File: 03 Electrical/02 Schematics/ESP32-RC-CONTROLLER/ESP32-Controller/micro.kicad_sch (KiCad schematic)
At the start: 3 parts, among them J2 USB_C_Receptacle_USB2.0_14P, U1 ESP32-C3, U3 CH340C

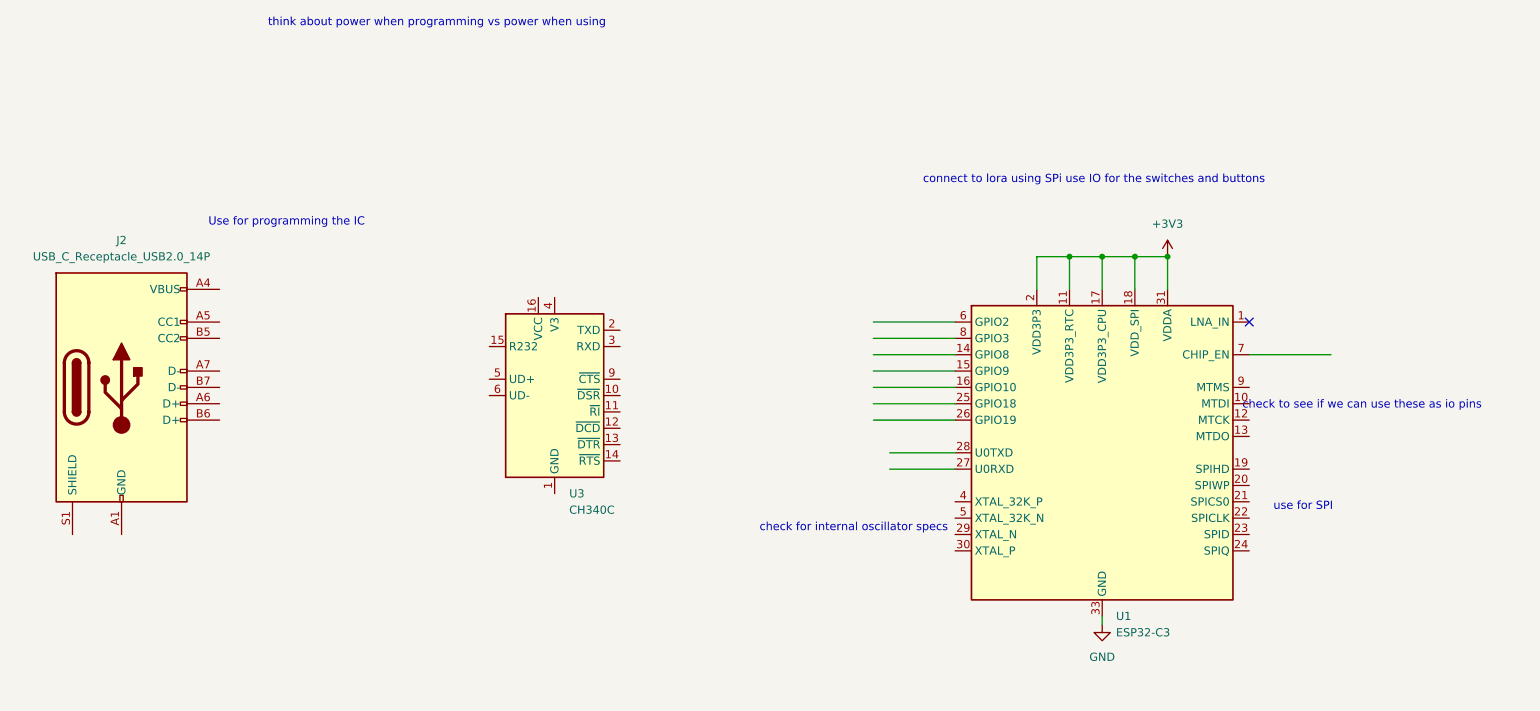
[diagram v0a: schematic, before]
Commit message: added new micro
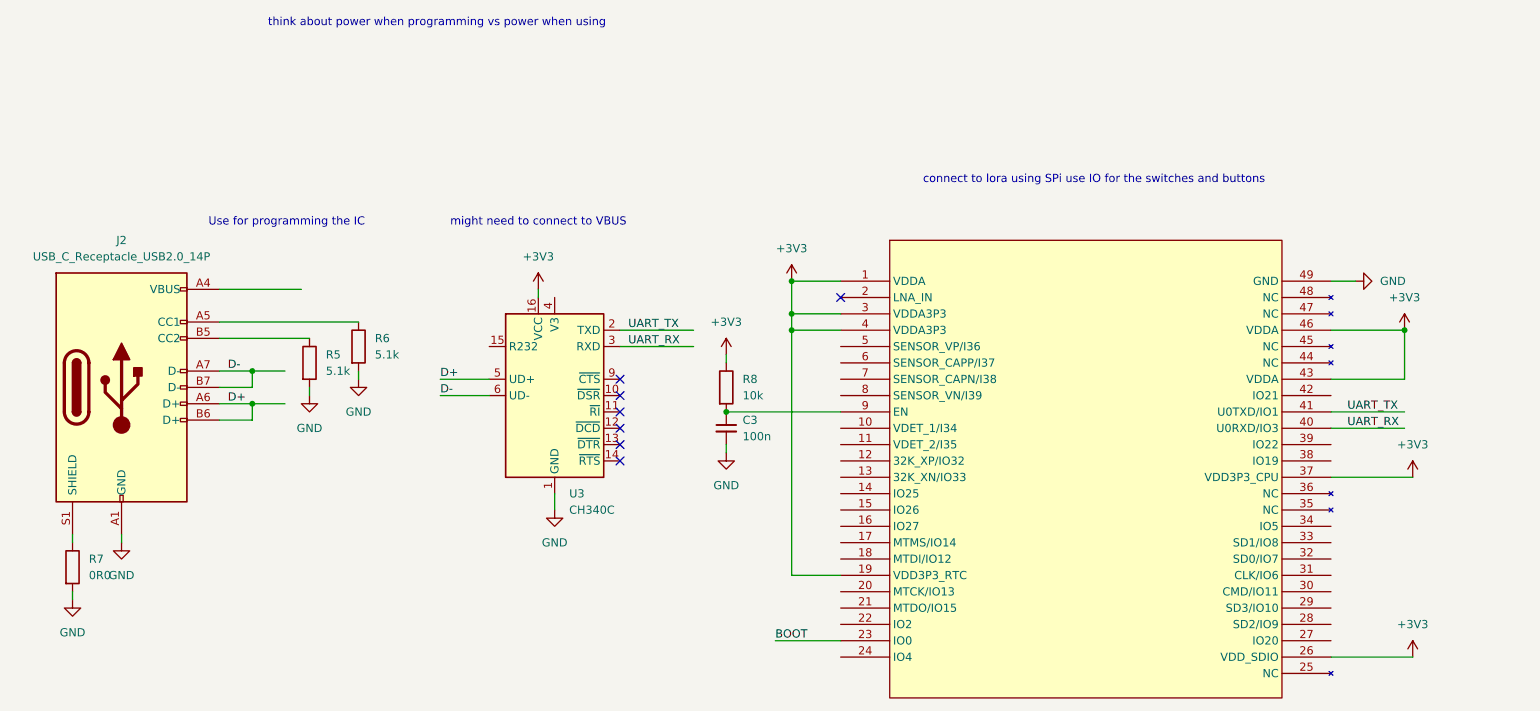
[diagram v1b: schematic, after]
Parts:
- removed U1: ESP32-C3, Package_DFN_QFN:QFN-32-1EP_5x5mm_P0.5mm_EP3.7x3.7mm, symbol MCU_Espressif:ESP32-C3
- added C3: 100n, Resistor_SMD:R_0402_1005Metric, symbol Device:C_Small
- added R5, R6: 5.1k, symbol Device:R
- added R7: 0R0, symbol Device:R
- added R8: 10k, symbol Device:R
- added U1: ~, Package_DFN_QFN:TQFN-48-1EP_7x7mm_P0.5mm_EP5.1x5.1mm_ThermalVias, symbol New_Library:ESP32-Pico_V3
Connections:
- net +3V3: now also U3.16 (VCC), R8.1, U1.1 (VDDA), U1.19 (VDD3P3_RTC), U1.26 (VDD_SDIO), U1.3 (VDDA3P3), U1.37 (VDD3P3_CPU), U1.4 (VDDA3P3), U1.43 (VDDA), U1.46 (VDDA)
- net GND: now also J2.A1 (GND), J2.A12 (GND), J2.B1 (GND), J2.B12 (GND), U3.1 (GND), C3.2, R5.2, R6.2, R7.2, U1.49 (GND)
- net at J2.A5 (CC1): now also R6.1
- net D+: now reaches J2.A6 (D+)
- net D+: now also J2.B6 (D+), U3.5 (UD+)
- net D-: now reaches J2.A7 (D-)
- net D-: now also J2.B7 (D-), U3.6 (UD-)
- net at J2.B5 (CC2): now also R5.1
- net at J2.S1 (SHIELD): now also R7.1
- net UART_TX: now reaches U3.2 (TXD)
- net UART_TX: now also U1.41 (U0TXD/IO1)
- net UART_RX: now reaches U3.3 (RXD)
- net UART_RX: now also U1.40 (U0RXD/IO3)
- new net: C3.1, R8.2, U1.9 (EN)
- new net BOOT: U1.23 (IO0)
- no-connect marks 1 -> 7
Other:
- note added: "might need to connect to VBUS"
- note removed: "check for internal oscillator specs"
- note removed: "check to see if we can use these as io pins"
- note removed: "use for SPI"
